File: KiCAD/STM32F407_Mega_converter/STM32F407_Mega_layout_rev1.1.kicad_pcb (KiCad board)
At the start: 2 copper layers, 102 x 53.8 mm, 94 parts, among them J1 Conn_01x08_Pin, J10 Conn_01x04_Pin, J2 Conn_01x08_Pin, J3 Conn_01x08_Pin, J4 Conn_01x08_Pin, J5 Conn_01x08_Pin, J6 Conn_01x10_Pin, J7 Conn_02x18, J8 MSD-1-A, J9 AU-Y1007, SW1 SW_Push, SW2 SW_Push, U1 STM32F407VGTx, U2 MCP6004, U3 AMS1117-3.3, U4 MCP6004, U5 MCP6004, U6 MCP6004, U7 MCP2551-I-SN, Y1 8Mhz, Y2 32.768KHz

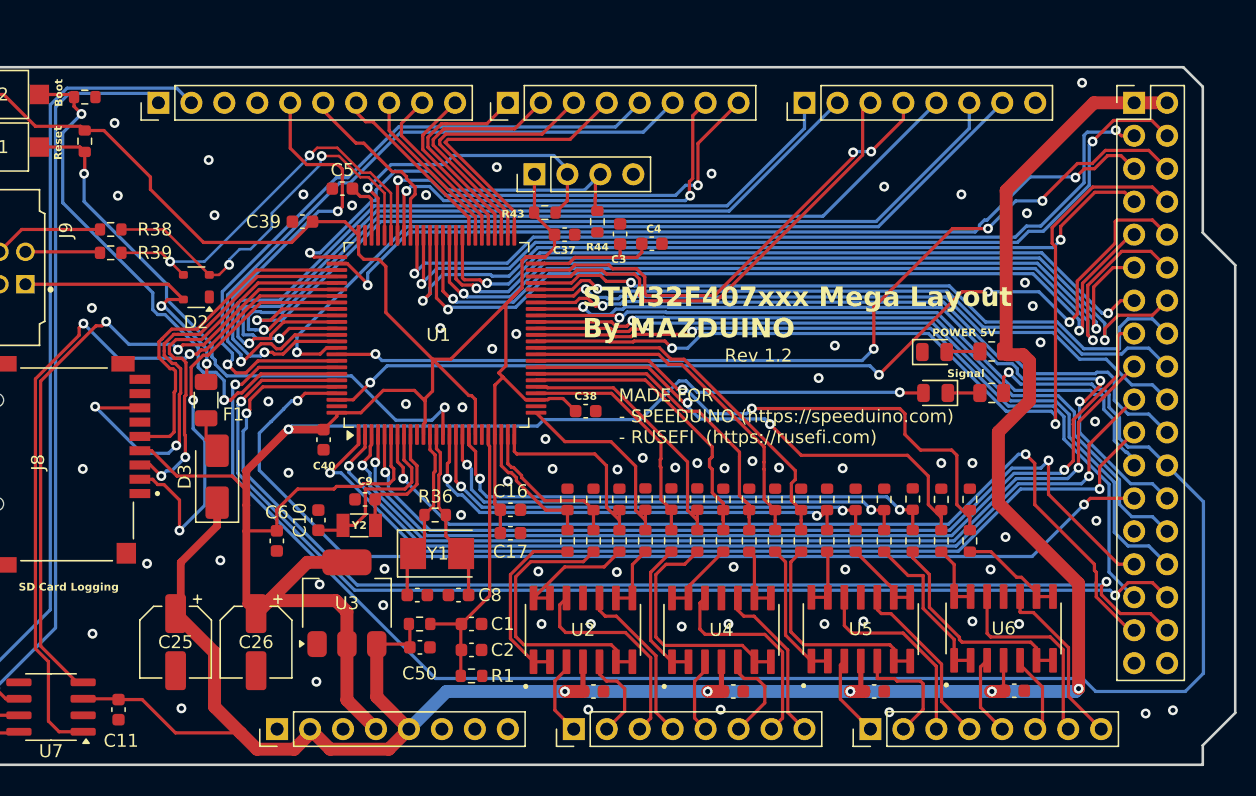
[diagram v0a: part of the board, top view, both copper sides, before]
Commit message: update rev1.2 fix sdcard conflict with ua4c board connector
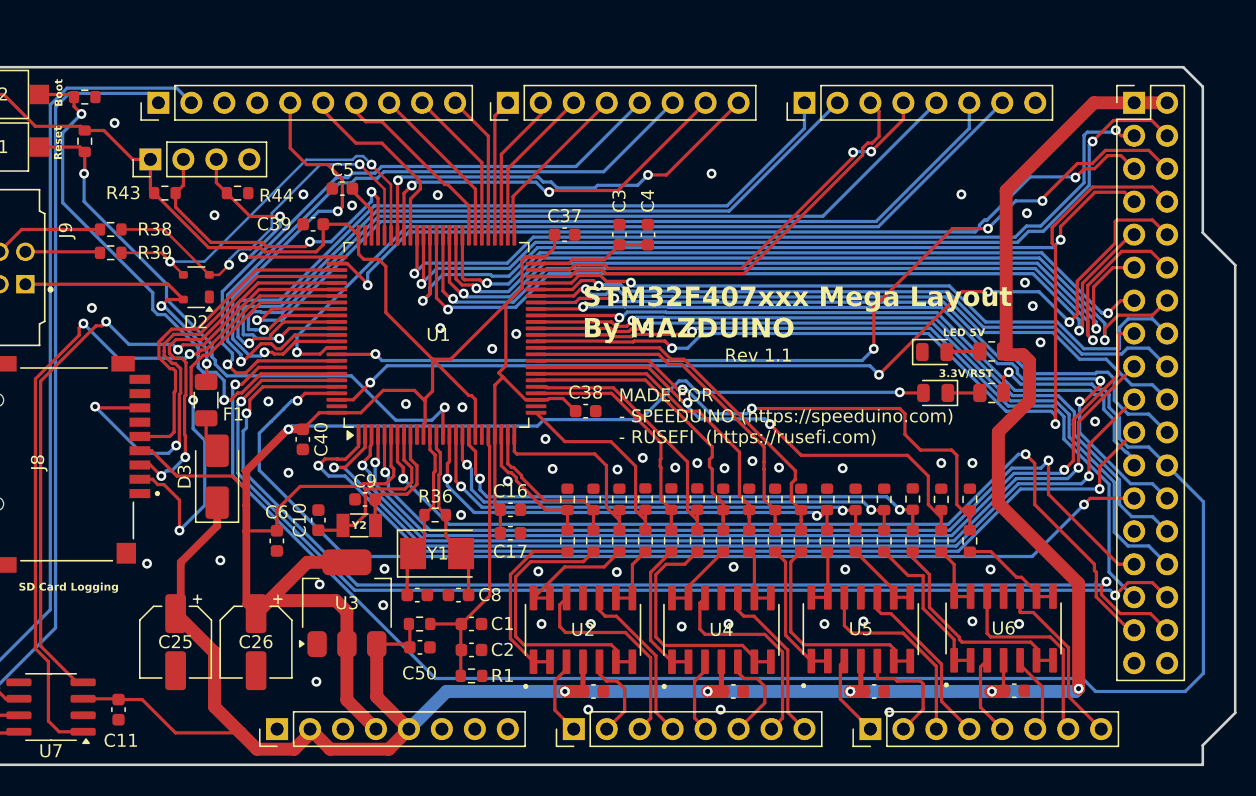
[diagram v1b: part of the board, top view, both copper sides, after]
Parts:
- moved J10 29.6 mm to (113.7, 76.6)
- moved R43 29.3 mm to (114.8, 79.2)
- moved R44 27.8 mm to (120.4, 79.2), turned to 0 degrees
- moved C40 1.60 mm to (125.4, 98.2)
- moved C39 0.85 mm to (126.2, 81.6)
- moved C4 0.76 mm to (152.0, 82.4), turned to -90 degrees
- moved C3 0.07 mm to (149.8, 82.4)
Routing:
- net /SWCLK: track 31.6 -> 19.6 mm, vias 1 -> 2
- net /D4: track 23.1 -> 13.2 mm
- net /D5: track 21.0 -> 12.3 mm
- net /D6: track 19.0 -> 11.5 mm
- net /D7: track 16.9 -> 10.6 mm
- net +3.3V: track 247.7 -> 242.9 mm
- net /TXD1: track 33.8 -> 30.0 mm
- net /RXD3: track 37.3 -> 34.8 mm
- net /RXD1: track 35.8 -> 33.7 mm
- net /D8: track 13.3 -> 11.3 mm
- net /D38: track 72.4 -> 74.3 mm
- net /D40: track 73.1 -> 75.0 mm
- net /TXD3: track 36.0 -> 34.3 mm
- net Net-(U1-VCAP_1): track 10.7 -> 9.23 mm
- net /SWDIO: track 24.6 -> 26.0 mm, vias 1 -> 2
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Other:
- board text added: "3.3V/RST"
- board text added: "LED 5V"
- board text added: "Rev 1.1"
- board text removed: "POWER 5V"
- board text removed: "Rev 1.2"
- board text removed: "Signal"
